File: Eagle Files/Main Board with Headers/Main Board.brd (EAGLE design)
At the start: 78.4 x 48.2 mm, 34 parts, among them Y1 16MHz

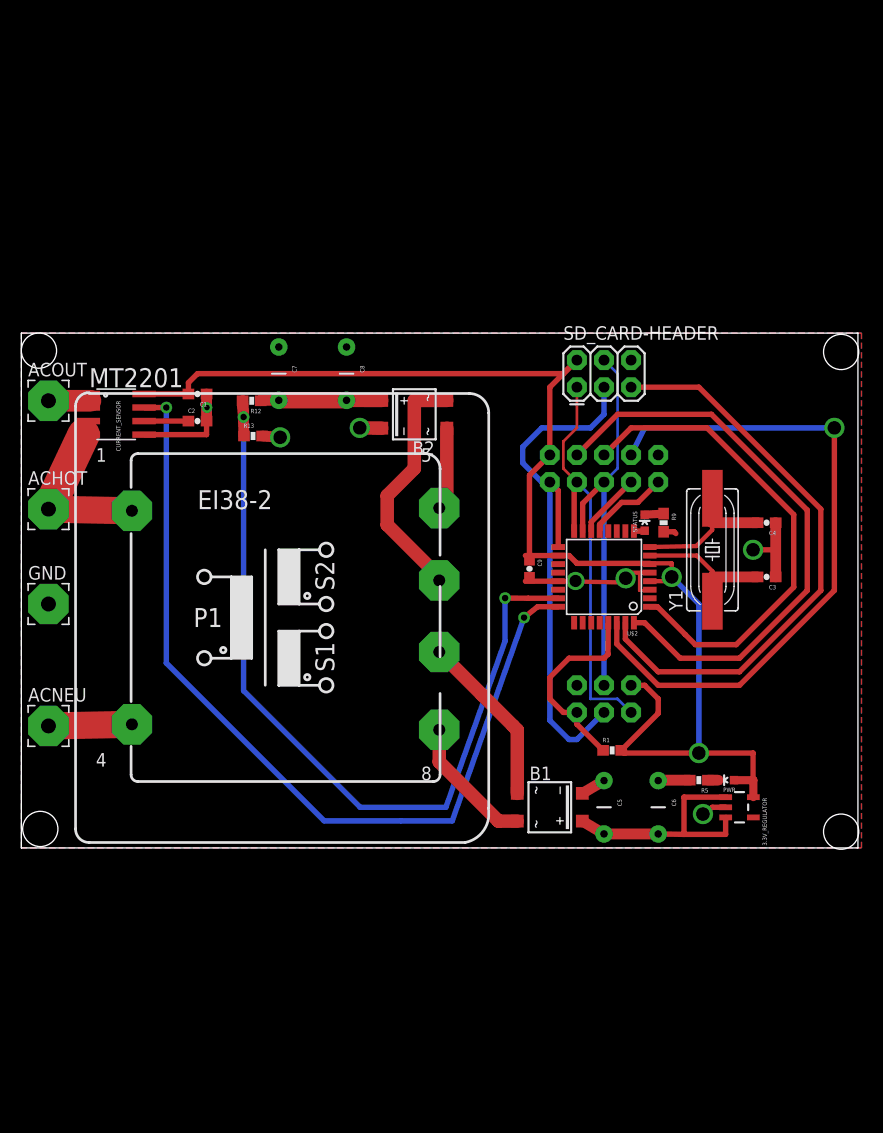
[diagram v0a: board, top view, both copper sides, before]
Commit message: More updates to the Main Board with Headers.
The transformer will now be under the board, so now we can place things inside that footprint on the top.

This saves us something around a square inch or two of board space.

--Arthur

git-svn-id: http://cd-net.net/CPE496/trunk@95 05b6d0e0-c345-4a8e-a5b7-579c8bd0b646
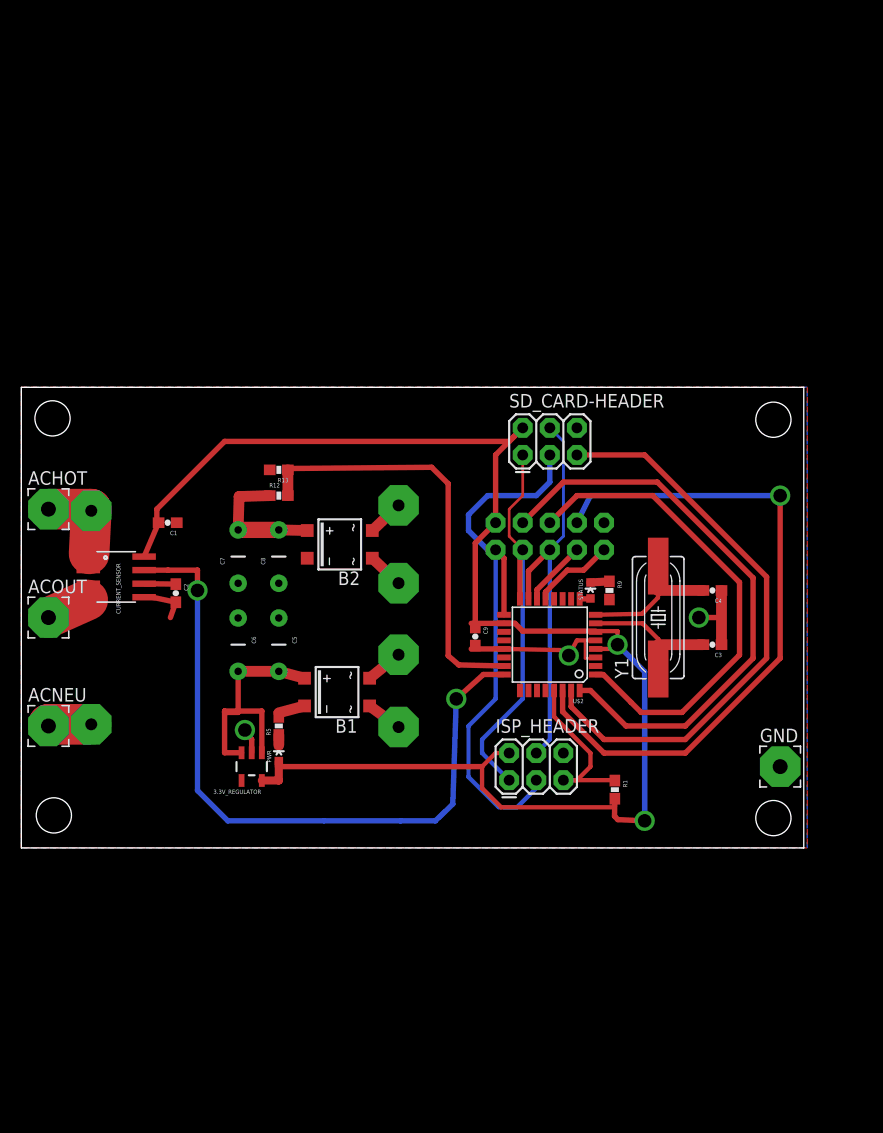
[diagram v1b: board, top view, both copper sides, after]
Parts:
- moved GND 70.3 mm to (71.1, 7.62)
- moved 3.3V_REGULATOR 45.9 mm to (21.6, 7.62), turned to 180 degrees
- moved C6 42.2 mm to (20.3, 19.1)
- moved PWR 42.0 mm to (24.1, 8.89), turned to 0 degrees
- moved R5 39.7 mm to (24.1, 11.4), turned to 90 degrees
- moved C5 34.1 mm to (24.1, 19.1)
- moved B1 22.7 mm to (29.6, 14.6), turned to 90 degrees
- moved ACOUT 20.3 mm to (2.54, 21.6)
- moved C8 18.3 mm to (24.1, 27.3), turned to 90 degrees
- moved C7 17.6 mm to (20.3, 27.3), turned to 90 degrees
- moved C2 16.3 mm to (14.5, 23.9), turned to 270 degrees
- moved CURRENT_SENSOR 15.2 mm to (8.89, 25.4)
- moved B2 14.1 mm to (29.8, 28.4)
- moved ISP_HEADER 13.1 mm to (45.7, 6.35), flipped to the top
- moved C1 12.4 mm to (13.7, 30.5)
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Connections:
- removed net N$8: ACOUT.1, CURRENT_SENSOR.1, CURRENT_SENSOR.2
- new net N$9: ACOUT.1, CURRENT_SENSOR.3, CURRENT_SENSOR.4
- net N$1: now also CURRENT_SENSOR.1, CURRENT_SENSOR.2, MT2201.4; no longer CURRENT_SENSOR.3, CURRENT_SENSOR.4, MT2201.1
- net N$2: now also MT2201.1; no longer MT2201.4
- net N$23: now also B1.~2, MT2201.6; no longer B1.~1, MT2201.7
- net N$3: now also B1.~1, MT2201.5; no longer B1.~2, MT2201.8
- net N$4: now also MT2201.7; no longer MT2201.5
- net N$5: now also MT2201.8; no longer MT2201.6
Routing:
- net PC0: track 79.5 -> 40.3 mm, vias 2 -> 0
- net N$5: track 23.3 -> 3.41 mm
- net 3.3V: track 127.3 -> 145.5 mm
- net PC1: track 82.7 -> 66.6 mm
- net GND: track 50.1 -> 36.9 mm, vias 7 -> 3
- net N$23: track 16.3 -> 3.50 mm
- net N$3: track 12.6 -> 3.36 mm
- net N$1: track 17.3 -> 10.4 mm
- net N$9: track 0.00 -> 6.00 mm
- net N$8: track 5.87 -> 0.00 mm
- net N$4: track 8.20 -> 3.39 mm
- net N$2: track 7.82 -> 4.17 mm
- net RESET: track 19.0 -> 16.5 mm
- net SCK: track 51.8 -> 54.0 mm
- net UNREGULATED_VCC: track 22.7 -> 24.4 mm
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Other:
- board size 78.4 x 48.2 mm -> 73.3 x 43.2 mm

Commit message: Latest Update to all the boards.
--Arthur

git-svn-id: http://cd-net.net/CPE496/trunk@96 05b6d0e0-c345-4a8e-a5b7-579c8bd0b646
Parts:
- moved GND 1.80 mm to (69.8, 8.89)

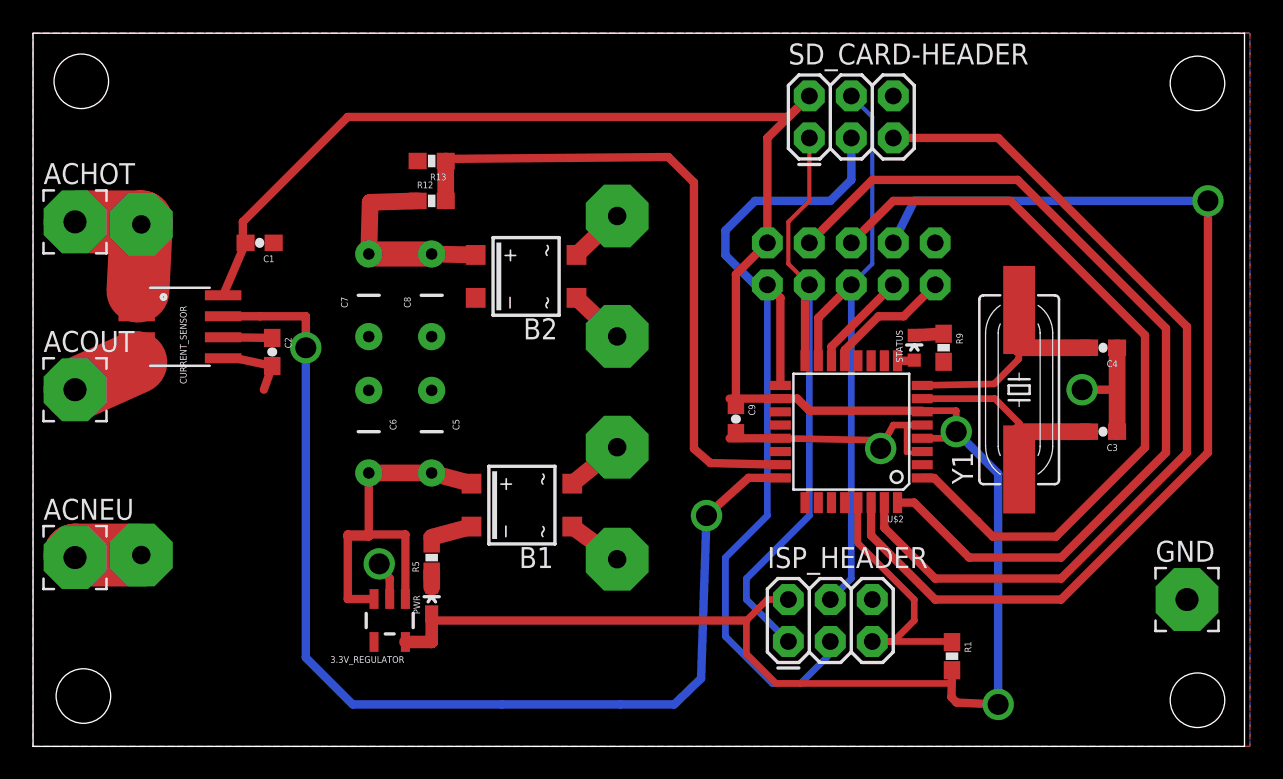
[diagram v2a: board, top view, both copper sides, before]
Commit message: Updated "Main Board with Headers" so the ground plane is safely away from AC power.
--Arthur

git-svn-id: http://cd-net.net/CPE496/trunk@102 05b6d0e0-c345-4a8e-a5b7-579c8bd0b646
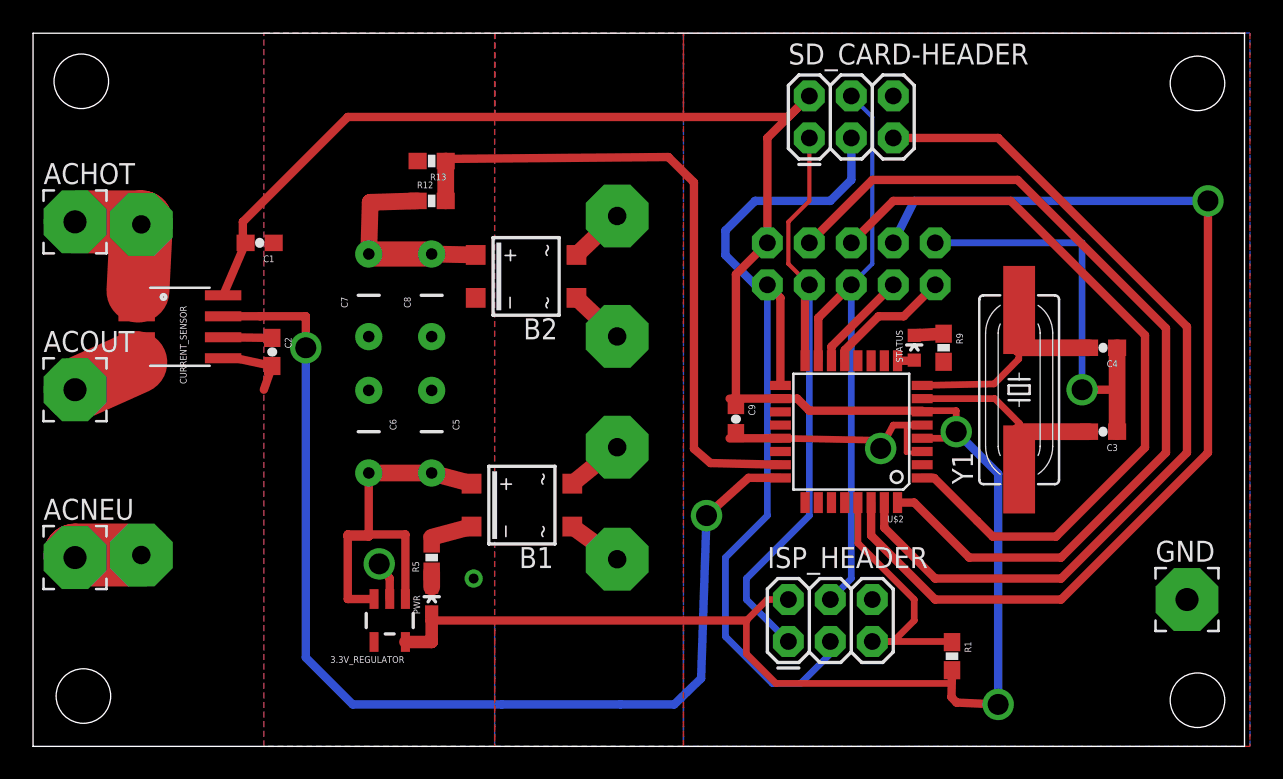
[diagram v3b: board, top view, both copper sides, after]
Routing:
- net GND: track 36.9 -> 54.7 mm, vias 3 -> 4
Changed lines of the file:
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@@
 <layers>
 <layer number="1" name="Top" color="4" fill="1" visible="yes" active="yes"/>
-<layer number="16" name="Bottom" color="1" fill="1" visible="no" active="yes"/>
-<layer number="17" name="Pads" color="2" fill="1" visible="yes" active="yes"/>
-<layer number="18" name="Vias" color="2" fill="1" visible="yes" active="yes"/>
+<layer number="16" name="Bottom" color="1" fill="1" visible="yes" active="yes"/>
+<layer number="17" name="Pads" color="2" fill="1" visible="no" active="yes"/>
+<layer number="18" name="Vias" color="2" fill="1" visible="no" active="yes"/>
 <layer number="19" name="Unrouted" color="6" fill="1" visible="no" active="yes"/>
 <layer number="20" name="Dimension" color="15" fill="1" visible="no" active="yes"/>
@@
 <wire x1="65.62" y1="24.13" x2="65.532" y2="24.13" width="0.254" layer="1"/>
 <wire x1="14.478" y1="23.026" x2="12.28" y2="23.495" width="0.508" layer="1"/>
-<polygon width="0.254" layer="16" isolate="0.635" thermals="no">
+<polygon width="0.254" layer="16" isolate="0.635" orphans="yes" thermals="no">
 <vertex x="73.66" y="43.18"/>
-<vertex x="0" y="43.18"/>
-<vertex x="0" y="0"/>
+<vertex x="39.37" y="43.18"/>
+<vertex x="39.37" y="0"/>
 <vertex x="73.66" y="0"/>
 </polygon>
@@
 <contactref element="RADIO-HEADER" pad="9"/>
 <contactref element="SD_CARD-HEADER" pad="6"/>
-<polygon width="0.508" layer="1" isolate="0.635" thermals="no">
-<vertex x="0" y="43.18"/>
+<polygon width="0.508" layer="1" isolate="0.635" orphans="yes" thermals="no">
+<vertex x="39.37" y="43.18"/>
 <vertex x="73.66" y="43.18"/>
 <vertex x="73.66" y="0"/>
-<vertex x="0" y="0"/>
+<vertex x="39.37" y="0"/>
 </polygon>
 <wire x1="24.13" y1="12.66" x2="26.541" y2="13.305" width="1.016" layer="1"/>
 <wire x1="14.478" y1="23.026" x2="13.97" y2="21.59" width="0.508" layer="1"/>
+<polygon width="0.4064" layer="1" isolate="0.635" orphans="yes" thermals="no">
+<vertex x="13.97" y="0"/>
+<vertex x="13.97" y="43.18"/>
+<vertex x="27.94" y="43.18"/>
+<vertex x="27.94" y="0"/>
+</polygon>
+<via x="26.67" y="10.16" extent="1-16" drill="0.6" shape="square"/>
+<polygon width="0.4064" layer="1" isolate="0.635" orphans="yes" thermals="no">
+<vertex x="39.37" y="38.1"/>
+<vertex x="39.37" y="43.18"/>
+<vertex x="27.94" y="43.18"/>
+<vertex x="27.94" y="38.1"/>
+</polygon>
+<polygon width="0.4064" layer="16" isolate="0.635" orphans="yes" thermals="no">
+<vertex x="13.97" y="0"/>
+<vertex x="13.97" y="43.18"/>
+<vertex x="27.94" y="43.18"/>
+<vertex x="27.94" y="0"/>
+</polygon>
+<polygon width="0.4064" layer="16" isolate="0.635" orphans="yes" thermals="no">
+<vertex x="27.94" y="43.18"/>
+<vertex x="27.94" y="38.1"/>
+<vertex x="39.37" y="38.1"/>
+<vertex x="39.37" y="43.18"/>
+</polygon>
+<polygon width="0.4064" layer="16" isolate="0.635" orphans="yes" thermals="no">
+<vertex x="27.94" y="0"/>
+<vertex x="27.94" y="7.62"/>
+<vertex x="39.37" y="7.62"/>
+<vertex x="39.37" y="0"/>
+</polygon>
+<polygon width="0.4064" layer="1" isolate="0.635" orphans="yes" thermals="no">
+<vertex x="27.94" y="7.62"/>
+<vertex x="27.94" y="0"/>
+<vertex x="39.37" y="0"/>
+<vertex x="39.37" y="7.62"/>
+</polygon>
+<wire x1="54.61" y1="30.48" x2="63.5" y2="30.48" width="0.4064" layer="16"/>
+<wire x1="63.5" y1="30.48" x2="63.5" y2="21.59" width="0.4064" layer="16"/>
+<wire x1="63.5" y1="21.59" x2="52.07" y2="39.37" width="0" layer="19" extent="1-16"/>
 </signal>
 <signal name="MOSI">

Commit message: Headers board now has the SD Card holder integrated into it.
This saves us board space, and brings us one step closer to a nice integrated board.

--Arthur

git-svn-id: http://cd-net.net/CPE496/trunk@115 05b6d0e0-c345-4a8e-a5b7-579c8bd0b646
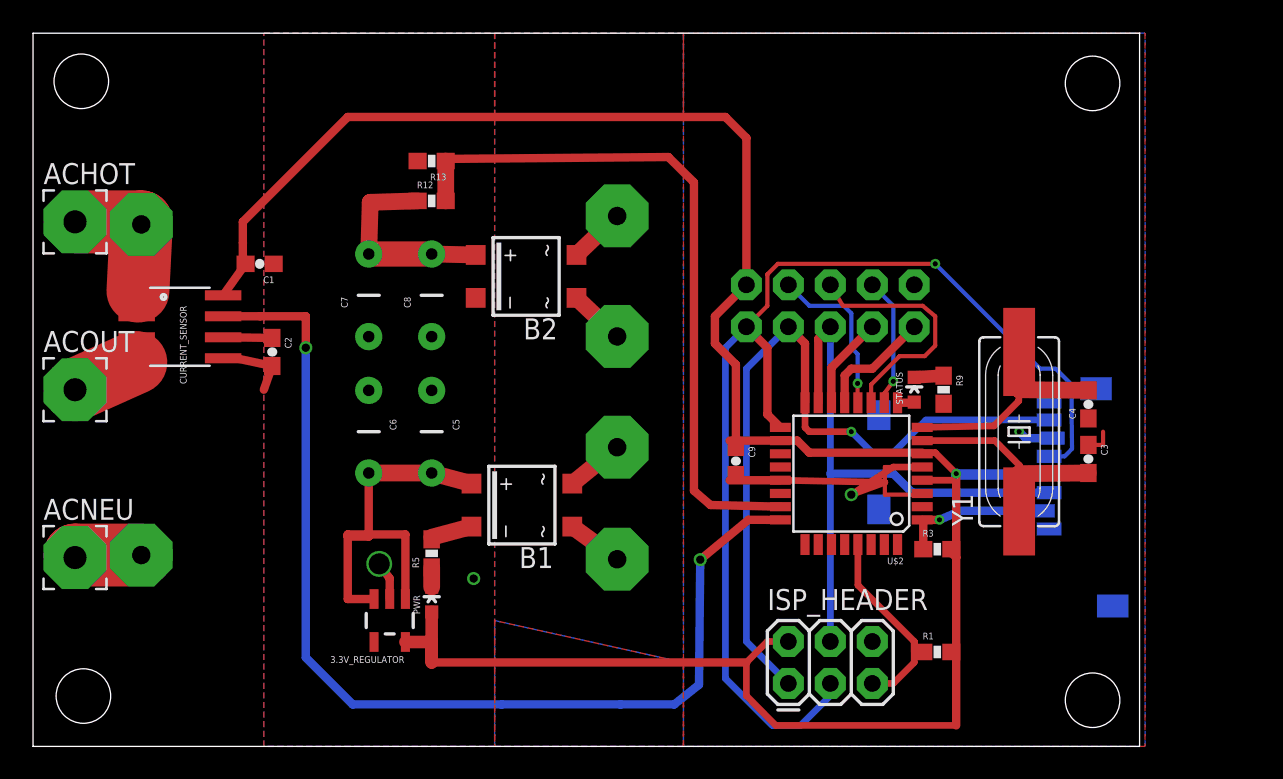
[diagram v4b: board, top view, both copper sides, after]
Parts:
- removed GND: (no value), wirepad:3,81/1,4
- removed SD_CARD-HEADER: AVR_SPI_PRG_6PTH, SparkFun:2X3
- added R3: 10K, SparkFun:0603-RES
- added U$1: MICROSD, group10:MICRO-SD-SOCKET-PP
- moved JP2 6.35 mm to (64.1, 40.1)
- moved JP4 6.35 mm to (64.1, 2.79)
- moved C4 3.54 mm to (63.9, 20.7), turned to 90 degrees
- moved RADIO-HEADER 2.84 mm to (48.3, 26.7)
- moved C9 2.54 mm to (42.5, 17.3)
- moved ISP_HEADER 2.54 mm to (45.7, 3.81)
- moved R9 2.54 mm to (55.1, 21.6)
- moved STATUS 2.54 mm to (53.3, 21.6)
- moved U$2 2.54 mm to (49.5, 16.5)
- moved Y1 2.54 mm to (59.7, 19.1)
- moved C3 1.88 mm to (63.9, 17.4), turned to 270 degrees
- moved C1 1.27 mm to (13.7, 29.2)
- moved R1 0.92 mm to (54.7, 5.71), turned to 0 degrees
- moved R5 0.25 mm to (24.1, 11.7)
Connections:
- removed net CLKM: U$2.10
- removed net N/C: U$2.2
- net 3.3V: now also R3.2, U$1.4; no longer SD_CARD-HEADER.2
- net CS-SD_CARD: now also R3.1, U$1.2, U$2.1; no longer SD_CARD-HEADER.5, U$2.31
- net DIG2: now also U$2.11; no longer U$2.1
- net GND: now also U$1.6; no longer GND.1, SD_CARD-HEADER.6
- net MISO: now also U$1.7; no longer SD_CARD-HEADER.1
- net MOSI: now also U$1.3; no longer SD_CARD-HEADER.4
- net RADIO-RST: now also U$2.10; no longer U$2.30
- net SCK: now also U$1.5; no longer SD_CARD-HEADER.3
- net SLP_TR: now also U$2.12; no longer U$2.32
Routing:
- net RADIO-RST: track 63.5 -> 7.84 mm
- net CS-SD_CARD: track 54.4 -> 9.19 mm, vias 0 -> 1
- net SLP_TR: track 54.7 -> 10.1 mm, vias 0 -> 1
- net DIG2: track 46.2 -> 15.0 mm
- net GND: track 54.7 -> 36.4 mm
- net SCK: track 54.0 -> 68.6 mm, vias 0 -> 1
- net MISO: track 38.9 -> 46.8 mm, vias 0 -> 1
- net RESET: track 16.5 -> 12.8 mm
- net PC0: track 40.3 -> 42.8 mm
- net PC1: track 66.6 -> 64.3 mm
- net 3.3V: track 145.5 -> 146.9 mm, vias 2 -> 1
- net IRQ: track 7.76 -> 7.09 mm
- net CS-RADIO: track 6.15 -> 5.62 mm
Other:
- board size 73.3 x 43.2 mm -> 67 x 43.2 mm
